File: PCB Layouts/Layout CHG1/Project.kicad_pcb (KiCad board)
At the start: 2 copper layers, 15 x 17.5 mm, 10 parts, among them J1 Conn_01x04

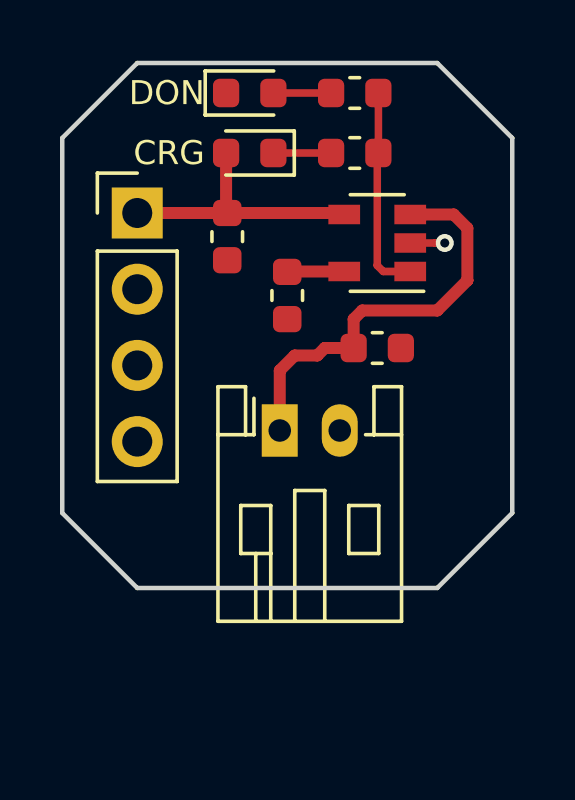
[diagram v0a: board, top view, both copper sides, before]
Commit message: Updated Lipo charger PCB to include changeover diode so that the battery can be used to power the circuit in the absence of an external power supply
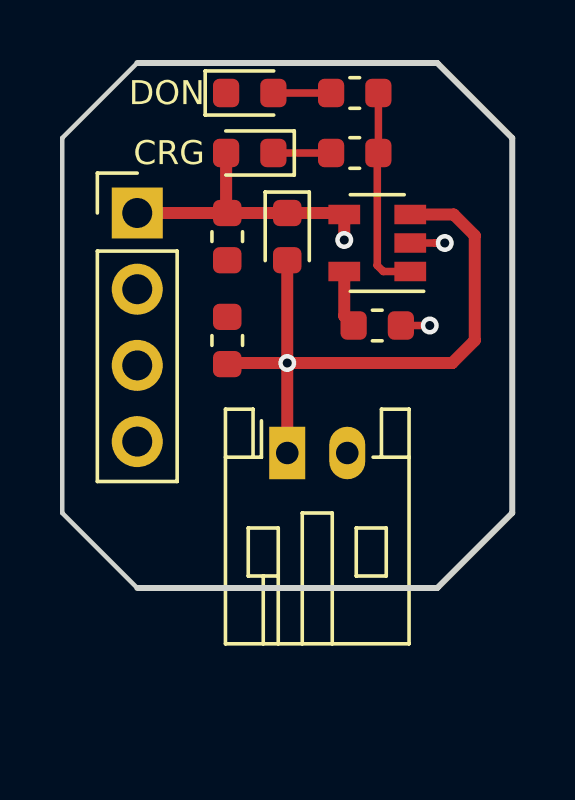
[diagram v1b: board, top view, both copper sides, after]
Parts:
- added D3: DONE, LED_SMD:LED_0603_1608Metric, F.Cu at (103.8, 96.0)
- D1: value CRG -> D; footprint LED_SMD:LED_0603_1608Metric -> Diode_SMD:D_0603_1608Metric
- D2: value DONE -> CHG
- RREF1: value 2k -> 5k
- moved C2 5.01 mm to (103.0, 104.2), turned to 90 degrees
- moved RREF1 3.16 mm to (108.0, 103.8), turned to 180 degrees
- moved D1 3.05 mm to (105.0, 100.8), turned to 270 degrees
- moved D2 2.00 mm to (103.8, 98.0), turned to 180 degrees
- moved JSTPH1 0.79 mm to (105.0, 108.0)
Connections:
- net Net-(CGU1-Pad1) renamed STAT
- net Net-(CGU1-Pad5) renamed PROG
- D1 pad 1: Net-(D1-Pad1) -> VDD
- D1 pad 2: VDD -> VBAT
- D2 pad 1: GND -> Net-(D2-Pad1)
- D2 pad 2: Net-(D2-Pad2) -> VDD
- R2 pad 2: Net-(D1-Pad1) -> Net-(D2-Pad1)
- R3 pad 2: Net-(D2-Pad2) -> Net-(D3-Pad2)
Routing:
- net VBAT: track 13.9 -> 20.9 mm, vias 0 -> 1
- net Net-(D3-Pad2): track 0.00 -> 1.93 mm
- net Net-(D2-Pad2): track 1.93 -> 0.00 mm
- net Net-(D2-Pad1): track 0.00 -> 1.93 mm
- net Net-(D1-Pad1): track 1.93 -> 0.00 mm
- net GND: track 1.87 -> 2.83 mm, vias 1 -> 2
- net VDD: track 8.97 -> 9.82 mm, vias 0 -> 1

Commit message: Moved the diode on Lipo charger layout
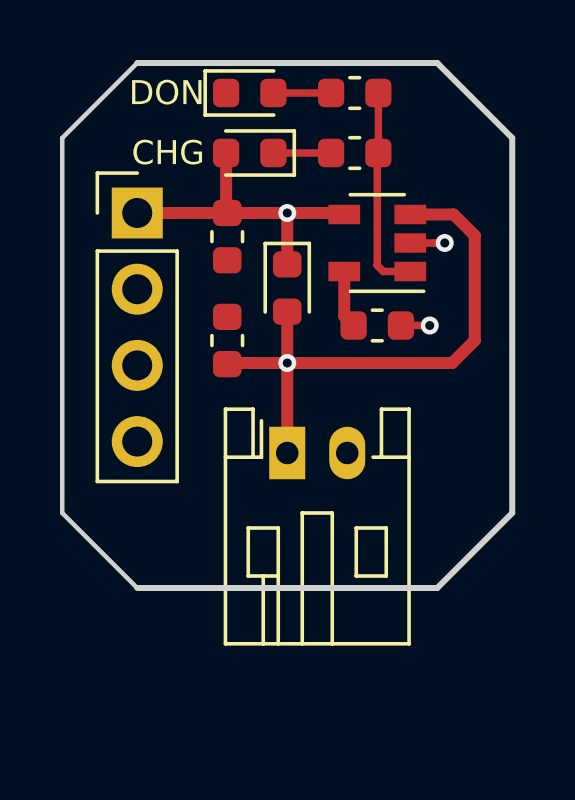
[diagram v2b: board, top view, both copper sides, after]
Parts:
- moved D1 1.71 mm to (105.0, 102.5)
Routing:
- net VBAT: track 20.9 -> 19.2 mm
- net VDD: track 9.82 -> 10.7 mm
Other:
- board text added: "CHG"
- board text removed: "CRG"
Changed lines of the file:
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@@
     (thickness 1.6)
     (drawings 12)
-    (tracks 39)
+    (tracks 40)
     (zones 0)
     (modules 11)
@@
   )
   (module Diode_SMD:D_0603_1608Metric (layer F.Cu)
-    (at 105 100.7875 270)
+    (at 105 102.5 270)
     (descr "Diode SMD 0603 (1608 Metric), square (rectangular) end terminal, IPC_7351 nominal, (Body size source: http://www.tortai-tech.com/upload/download/2011102023233369053.pdf), generated with kicad-footprint-generator")
     (tags diode)
@@
     (effects (font (size 1 1) (thickness 0.2)) (justify right mirror))
   )
-  (gr_text CRG (at 102.25 98) (layer F.SilkS)
+  (gr_text CHG (at 102.25 98) (layer F.SilkS)
     (effects (font (size 0.8 0.8) (thickness 0.15)) (justify right))
   )
@@
   (segment (start 102.9625 98) (end 102.9625 99.9625) (width 0.4) (layer F.Cu) (net 2))
   (segment (start 106.85 100) (end 106.9 100.05) (width 0.4) (layer F.Cu) (net 2))
-  (segment (start 103 100) (end 106.85 100) (width 0.4) (layer F.Cu) (net 2))
-  (segment (start 106.9 100.05) (end 106.9 100.9) (width 0.4) (layer F.Cu) (net 2))
-  (segment (start 106.9 100.9) (end 106.9 100.9) (width 0.4) (layer F.Cu) (net 2))
-  (via (at 106.9 100.9) (size 0.6) (drill 0.3) (layers F.Cu B.Cu) (net 2))
+  (segment (start 103 100) (end 105 100) (width 0.4) (layer F.Cu) (net 2))
+  (segment (start 105 100) (end 106.85 100) (width 0.4) (layer F.Cu) (net 2))
+  (segment (start 105 101.7125) (end 105 100) (width 0.4) (layer F.Cu) (net 2))
+  (segment (start 105 100) (end 105 100) (width 0.4) (layer F.Cu) (net 2))
+  (via (at 105 100) (size 0.6) (drill 0.3) (layers F.Cu B.Cu) (net 2))
   (segment (start 109.1 100.05) (end 110.55 100.05) (width 0.4) (layer F.Cu) (net 3))
   (segment (start 110.5 105) (end 109.25 105) (width 0.4) (layer F.Cu) (net 3))
@@
   (segment (start 109.25 105) (end 105 105) (width 0.4) (layer F.Cu) (net 3))
   (segment (start 105 105) (end 105 108) (width 0.4) (layer F.Cu) (net 3))
-  (segment (start 105 101.575) (end 105 105) (width 0.4) (layer F.Cu) (net 3))
   (segment (start 105 105) (end 105 105) (width 0.4) (layer F.Cu) (net 3))
   (via (at 105 105) (size 0.6) (drill 0.3) (layers F.Cu B.Cu) (net 3))
   (segment (start 103.0375 105) (end 103 105.0375) (width 0.4) (layer F.Cu) (net 3))
   (segment (start 105 105) (end 103.0375 105) (width 0.4) (layer F.Cu) (net 3))
-  (segment (start 106.4625 98) (end 104.5375 98) (width 0.254) (layer F.Cu) (net 8))
-  (segment (start 104.5375 96) (end 106.4625 96) (width 0.254) (layer F.Cu) (net 9))
+  (segment (start 105 103.2875) (end 105 105) (width 0.4) (layer F.Cu) (net 3))
   (segment (start 108.0375 98) (end 108.0375 96) (width 0.254) (layer F.Cu) (net 6))
   (segment (start 108 98.0375) (end 108.0375 98) (width 0.254) (layer F.Cu) (net 6))
@@
   (segment (start 106.9 103.4375) (end 107.2125 103.75) (width 0.4) (layer F.Cu) (net 7))
   (segment (start 106.9 101.95) (end 106.9 103.4375) (width 0.4) (layer F.Cu) (net 7))
+  (segment (start 106.4625 98) (end 104.5375 98) (width 0.254) (layer F.Cu) (net 8))
+  (segment (start 104.5375 96) (end 106.4625 96) (width 0.254) (layer F.Cu) (net 9))
   (zone (net 1) (net_name GND) (layer F.Cu) (hatch edge 0.508)
     (connect_pads (clearance 0.508))

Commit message: Added custom JST Lipo Header to Lipo Charging Layout
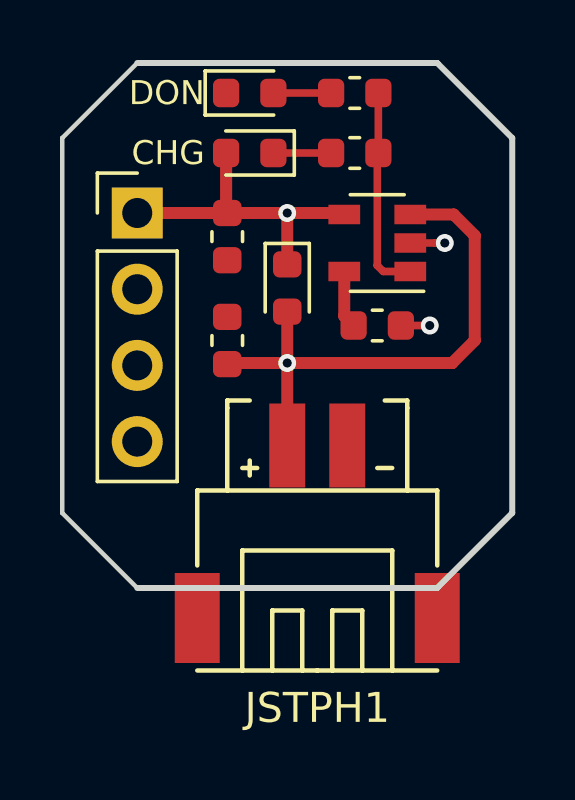
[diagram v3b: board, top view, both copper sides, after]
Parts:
- JSTPH1: footprint Connector_JST:JST_PH_S2B-PH-K_1x02_P2.00mm_Horizontal -> Custom_Footprint_Library:JST Lipo Header (S2B-PH-SM4-TB)
- moved JSTPH1 4.37 mm to (106.0, 112.2)
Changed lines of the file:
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@@
-    )
-  )
-  (module Connector_JST:JST_PH_S2B-PH-K_1x02_P2.00mm_Horizontal (layer F.Cu)
-    (at 105 108)
-    (descr "JST PH series connector, S2B-PH-K (http://www.jst-mfg.com/product/pdf/eng/ePH.pdf), generated with kicad-footprint-generator")
-    (tags "connector JST PH top entry")
-    (fp_text reference JSTPH1 (at 1 -2.55) (layer F.SilkS) hide
-      (effects (font (size 1 1) (thickness 0.15)))
-    )
-    (fp_text value Conn_01x02 (at 1 7.45) (layer F.Fab) hide
-      (effects (font (size 1 1) (thickness 0.15)))
-    )
-    (fp_line (start -0.86 0.14) (end -1.14 0.14) (layer F.SilkS) (width 0.12))
-    (fp_line (start -1.14 0.14) (end -1.14 -1.46) (layer F.SilkS) (width 0.12))
-    (fp_line (start -1.14 -1.46) (end -2.06 -1.46) (layer F.SilkS) (width 0.12))
-    (fp_line (start -2.06 -1.46) (end -2.06 6.36) (layer F.SilkS) (width 0.12))
-    (fp_line (start -2.06 6.36) (end 4.06 6.36) (layer F.SilkS) (width 0.12))
-    (fp_line (start 4.06 6.36) (end 4.06 -1.46) (layer F.SilkS) (width 0.12))
-    (fp_line (start 4.06 -1.46) (end 3.14 -1.46) (layer F.SilkS) (width 0.12))
-    (fp_line (start 3.14 -1.46) (end 3.14 0.14) (layer F.SilkS) (width 0.12))
-    (fp_line (start 3.14 0.14) (end 2.86 0.14) (layer F.SilkS) (width 0.12))
-    (fp_line (start 0.5 6.36) (end 0.5 2) (layer F.SilkS) (width 0.12))
-    (fp_line (start 0.5 2) (end 1.5 2) (layer F.SilkS) (width 0.12))
-    (fp_line (start 1.5 2) (end 1.5 6.36) (layer F.SilkS) (width 0.12))
-    (fp_line (start -2.06 0.14) (end -1.14 0.14) (layer F.SilkS) (width 0.12))
-    (fp_line (start 4.06 0.14) (end 3.14 0.14) (layer F.SilkS) (width 0.12))
-    (fp_line (start -1.3 2.5) (end -1.3 4.1) (layer F.SilkS) (width 0.12))
-    (fp_line (start -1.3 4.1) (end -0.3 4.1) (layer F.SilkS) (width 0.12))
-    (fp_line (start -0.3 4.1) (end -0.3 2.5) (layer F.SilkS) (width 0.12))
-    (fp_line (start -0.3 2.5) (end -1.3 2.5) (layer F.SilkS) (width 0.12))
-    (fp_line (start 3.3 2.5) (end 3.3 4.1) (layer F.SilkS) (width 0.12))
-    (fp_line (start 3.3 4.1) (end 2.3 4.1) (layer F.SilkS) (width 0.12))
-    (fp_line (start 2.3 4.1) (end 2.3 2.5) (layer F.SilkS) (width 0.12))
-    (fp_line (start 2.3 2.5) (end 3.3 2.5) (layer F.SilkS) (width 0.12))
-    (fp_line (start -0.3 4.1) (end -0.3 6.36) (layer F.SilkS) (width 0.12))
-    (fp_line (start -0.8 4.1) (end -0.8 6.36) (layer F.SilkS) (width 0.12))
-    (fp_line (start -2.45 -1.85) (end -2.45 6.75) (layer F.CrtYd) (width 0.05))
-    (fp_line (start -2.45 6.75) (end 4.45 6.75) (layer F.CrtYd) (width 0.05))
-    (fp_line (start 4.45 6.75) (end 4.45 -1.85) (layer F.CrtYd) (width 0.05))
-    (fp_line (start 4.45 -1.85) (end -2.45 -1.85) (layer F.CrtYd) (width 0.05))
-    (fp_line (start -1.25 0.25) (end -1.25 -1.35) (layer F.Fab) (width 0.1))
-    (fp_line (start -1.25 -1.35) (end -1.95 -1.35) (layer F.Fab) (width 0.1))
-    (fp_line (start -1.95 -1.35) (end -1.95 6.25) (layer F.Fab) (width 0.1))
-    (fp_line (start -1.95 6.25) (end 3.95 6.25) (layer F.Fab) (width 0.1))
-    (fp_line (start 3.95 6.25) (end 3.95 -1.35) (layer F.Fab) (width 0.1))
-    (fp_line (start 3.95 -1.35) (end 3.25 -1.35) (layer F.Fab) (width 0.1))
-    (fp_line (start 3.25 -1.35) (end 3.25 0.25) (layer F.Fab) (width 0.1))
-    (fp_line (start 3.25 0.25) (end -1.25 0.25) (layer F.Fab) (width 0.1))
-    (fp_line (start -0.86 0.14) (end -0.86 -1.075) (layer F.SilkS) (width 0.12))
-    (fp_line (start 0 0.875) (end -0.5 1.375) (layer F.Fab) (width 0.1))
-    (fp_line (start -0.5 1.375) (end 0.5 1.375) (layer F.Fab) (width 0.1))
-    (fp_line (start 0.5 1.375) (end 0 0.875) (layer F.Fab) (width 0.1))
-    (fp_text user %R (at 1 2.5) (layer F.Fab)
-      (effects (font (size 1 1) (thickness 0.15)))
-    )
-    (pad 1 thru_hole rect (at 0 0) (size 1.2 1.75) (drill 0.75) (layers *.Cu *.Mask)
-      (net 3 VBAT))
-    (pad 2 thru_hole oval (at 2 0) (size 1.2 1.75) (drill 0.75) (layers *.Cu *.Mask)
-      (net 1 GND))
-    (model ${KISYS3DMOD}/Connector_JST.3dshapes/JST_PH_S2B-PH-K_1x02_P2.00mm_Horizontal.wrl
-      (at (xyz 0 0 0))
-      (scale (xyz 1 1 1))
-      (rotate (xyz 0 0 0))
     )
   )
@@
       (rotate (xyz 0 0 0))
     )
+  )
+  (module "Custom_Footprint_Library:JST Lipo Header (S2B-PH-SM4-TB)" (layer F.Cu)
+    (at 106 112.25)
+    (fp_text reference JSTPH1 (at 0 4.25) (layer F.SilkS)
+      (effects (font (size 1 1) (thickness 0.15)))
+    )
+    (fp_text value Conn_01x02 (at 0 6) (layer F.Fab)
+      (effects (font (size 1 1) (thickness 0.15)))
+    )
+    (fp_line (start 0 3) (end -4 3) (layer F.SilkS) (width 0.15))
+    (fp_line (start 0 3) (end 4 3) (layer F.SilkS) (width 0.15))
+    (fp_line (start -4 -3) (end 4 -3) (layer F.SilkS) (width 0.15))
+    (fp_line (start -3 -3) (end -3 -5.75) (layer F.SilkS) (width 0.15))
+    (fp_line (start 3 -3) (end 3 -5.75) (layer F.SilkS) (width 0.15))
+    (fp_line (start -2.5 -3.75) (end -2 -3.75) (layer F.SilkS) (width 0.15))
+    (fp_line (start -2.25 -4) (end -2.25 -3.5) (layer F.SilkS) (width 0.15))
+    (fp_line (start 2 -3.75) (end 2.5 -3.75) (layer F.SilkS) (width 0.15))
+    (fp_line (start -3 -5.75) (end -3 -6) (layer F.SilkS) (width 0.15))
+    (fp_line (start -3 -6) (end -2.25 -6) (layer F.SilkS) (width 0.15))
+    (fp_line (start 3 -5.75) (end 3 -6) (layer F.SilkS) (width 0.15))
+    (fp_line (start 3 -6) (end 2.25 -6) (layer F.SilkS) (width 0.15))
+    (fp_line (start -1.5 3) (end -1.5 1) (layer F.SilkS) (width 0.15))
+    (fp_line (start -1.5 1) (end -0.5 1) (layer F.SilkS) (width 0.15))
+    (fp_line (start -0.5 1) (end -0.5 3) (layer F.SilkS) (width 0.15))
+    (fp_line (start 0.5 3) (end 0.5 1) (layer F.SilkS) (width 0.15))
+    (fp_line (start 0.5 1) (end 1.5 1) (layer F.SilkS) (width 0.15))
+    (fp_line (start 1.5 1) (end 1.5 3) (layer F.SilkS) (width 0.15))
+    (fp_line (start -2.5 3) (end -2.5 -1) (layer F.SilkS) (width 0.15))
+    (fp_line (start -2.5 -1) (end 2.5 -1) (layer F.SilkS) (width 0.15))
+    (fp_line (start 2.5 -1) (end 2.5 3) (layer F.SilkS) (width 0.15))
+    (fp_line (start 4 -3) (end 4 -0.5) (layer F.SilkS) (width 0.15))
+    (fp_line (start -4 -3) (end -4 -0.5) (layer F.SilkS) (width 0.15))
+    (pad 1 smd rect (at -1 -4.5) (size 1.2 2.8) (layers F.Cu F.Paste F.Mask)
+      (net 3 VBAT))
+    (pad 2 smd rect (at 1 -4.5) (size 1.2 2.8) (layers F.Cu F.Paste F.Mask)
+      (net 1 GND))
+    (pad "" connect rect (at -4 1.25) (size 1.5 3) (layers F.Cu F.Mask))
+    (pad "" connect rect (at 4 1.25) (size 1.5 3) (layers F.Cu F.Mask))
   )
   (gr_line (start 110 112.5) (end 100 112.5) (layer Edge.Cuts) (width 0.2))
@@
   (segment (start 110.55 100.05) (end 111.25 100.75) (width 0.4) (layer F.Cu) (net 3))
   (segment (start 109.25 105) (end 105 105) (width 0.4) (layer F.Cu) (net 3))
-  (segment (start 105 105) (end 105 108) (width 0.4) (layer F.Cu) (net 3))
   (segment (start 105 105) (end 105 105) (width 0.4) (layer F.Cu) (net 3))
   (via (at 105 105) (size 0.6) (drill 0.3) (layers F.Cu B.Cu) (net 3))
@@
   (segment (start 105 105) (end 103.0375 105) (width 0.4) (layer F.Cu) (net 3))
   (segment (start 105 103.2875) (end 105 105) (width 0.4) (layer F.Cu) (net 3))
+  (segment (start 105 107.75) (end 105 105) (width 0.4) (layer F.Cu) (net 3))
   (segment (start 108.0375 98) (end 108.0375 96) (width 0.254) (layer F.Cu) (net 6))
   (segment (start 108 98.0375) (end 108.0375 98) (width 0.254) (layer F.Cu) (net 6))
